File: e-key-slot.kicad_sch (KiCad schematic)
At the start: 27 parts, among them J1 MDT420E03002, J3 PJ-018, Q1 TSM9409CS, Q2 TSM9409CS, Q3 TSM9409CS, U1 TPS54331DRG4

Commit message: Add bounding boxes
Signed-off-by: JeffMboya <jangina.mboya@gmail.com>
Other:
- note added: "9v DC input"
- note added: "9v DC to 3v3 buck converter"
- note removed: "PCIe M.2 Key E Card Socket"
- moved on the sheet: J1

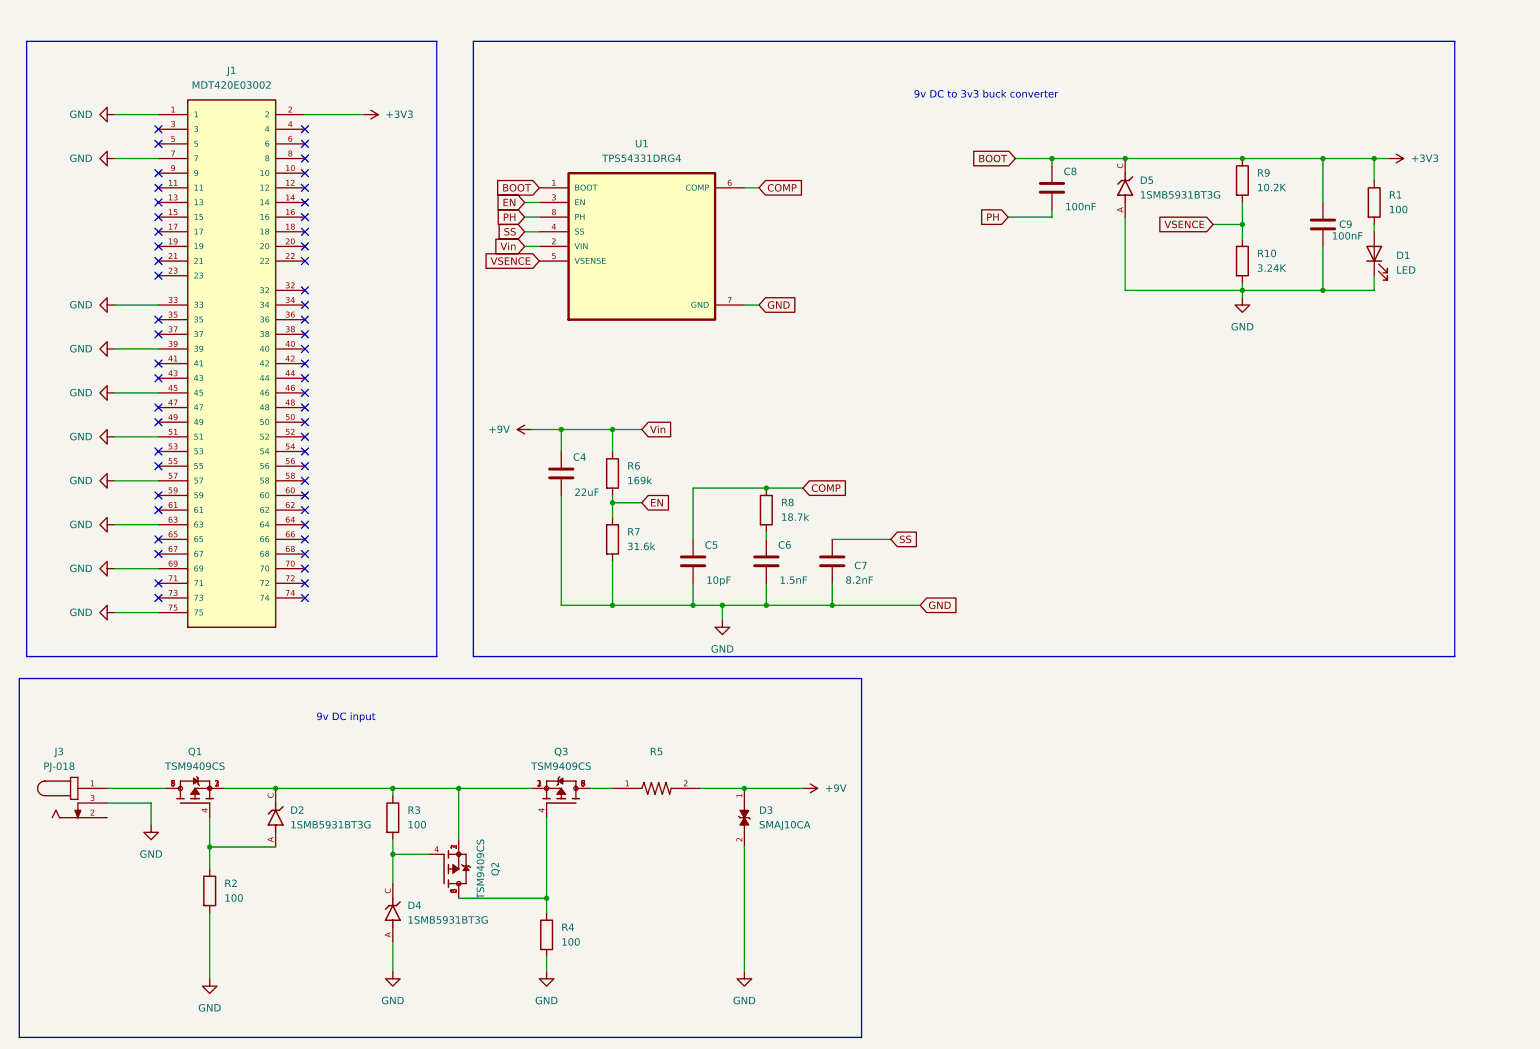
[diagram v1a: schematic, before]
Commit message: Add MCP73831
Signed-off-by: JeffMboya <jangina.mboya@gmail.com>
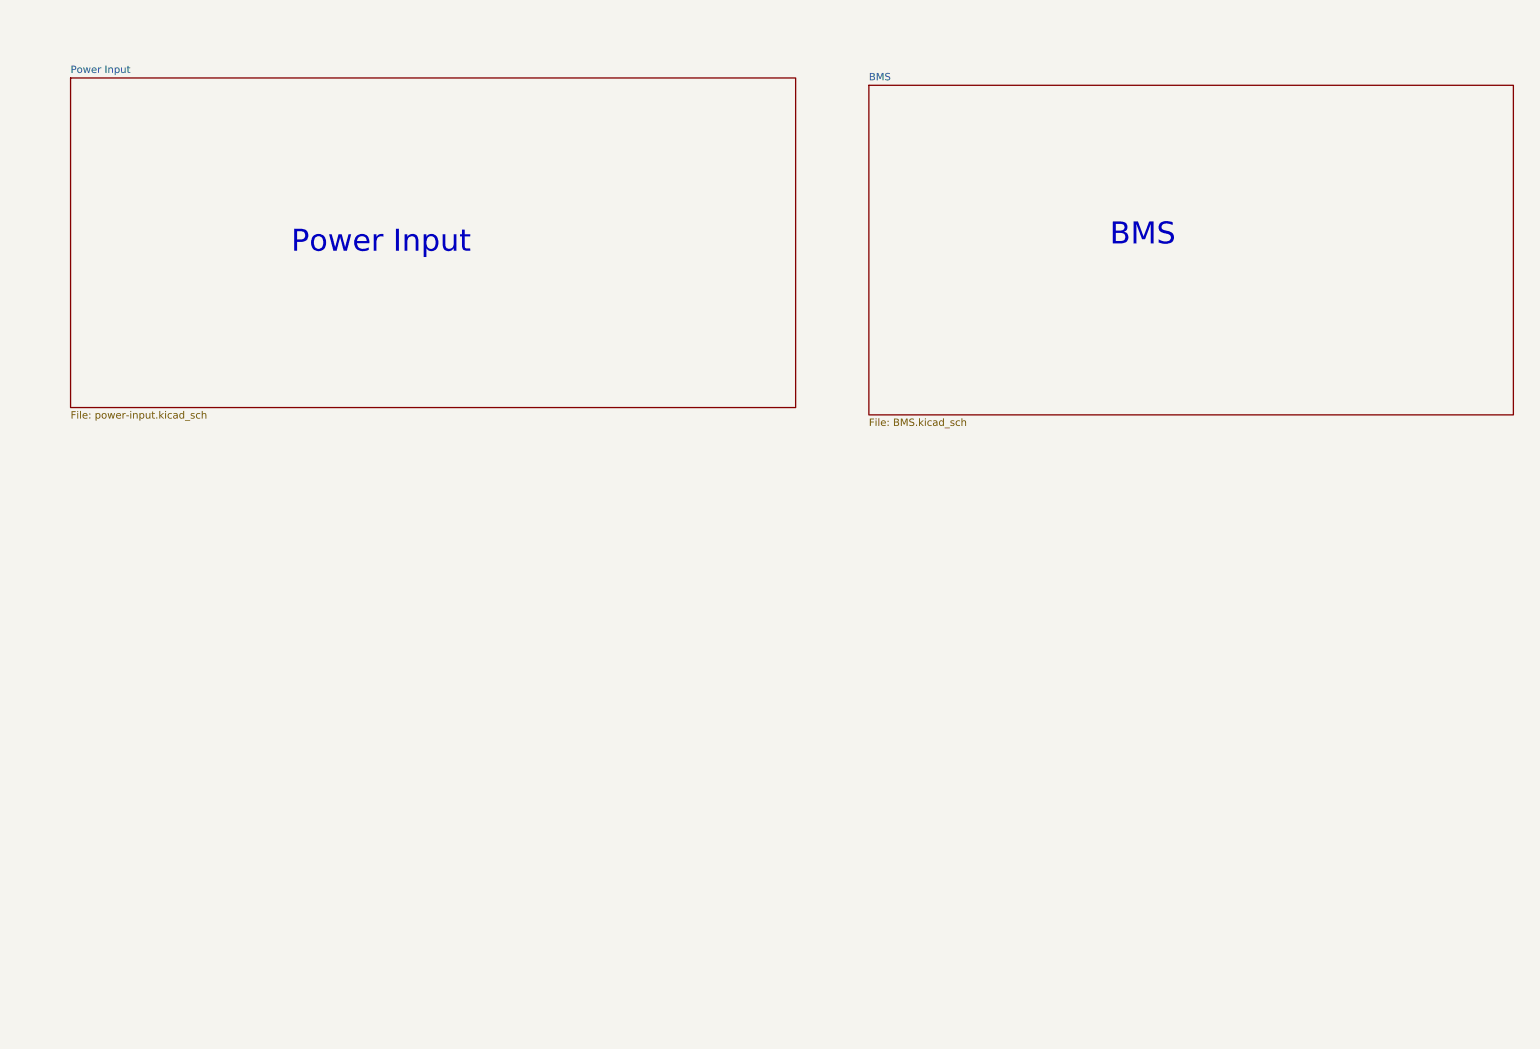
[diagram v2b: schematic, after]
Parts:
- removed C4: 22uF, Capacitor_SMD:C_1206_3216Metric, symbol Device:C
- removed C5: 10pF, Capacitor_SMD:C_1206_3216Metric, symbol Device:C
- removed C6: 1.5nF, Capacitor_SMD:C_1206_3216Metric, symbol Device:C
- removed C7: 8.2nF, Capacitor_SMD:C_1206_3216Metric, symbol Device:C
- removed C8, C9: 100nF, Capacitor_SMD:C_1206_3216Metric, symbol Device:C
- removed D1: LED, LED_SMD:LED_0603_1608Metric, symbol Device:LED
- removed D2, D4, D5: 1SMB5931BT3G, 1SMB5931BT3G:DIOM5436X247N, symbol 1SMB5931BT3G:1SMB5931BT3G
- removed D3: SMAJ10CA, SMAJ10CA:DIOM4325X250N, symbol SMAJ10CA:SMAJ10CA
- removed J1: MDT420E03002, MDT420E03002:AMPHENOL_MDT420E03002, symbol MDT420E03002:MDT420E03002
- removed J3: PJ-018, PJ-018:CUI_PJ-018, symbol PJ-018:PJ-018
- removed Q1, Q2, Q3: TSM9409CS, TSM9409CS:TRANS_TSM9409CS, symbol TSM9409CS:TSM9409CS
- removed R1, R2, R3, R4: 100, Resistor_SMD:R_0603_1608Metric, symbol Device:R
- removed R10: 3.24K, Resistor_SMD:R_0603_1608Metric, symbol Device:R
- removed R5: 0ZCA0100FF2E, 0ZCA0100FF2E:RESC3216X125N, symbol 0ZCA0100FF2E:0ZCA0100FF2E
- removed R6: 169k, Resistor_SMD:R_0603_1608Metric, symbol Device:R
- removed R7: 31.6k, Resistor_SMD:R_0603_1608Metric, symbol Device:R
- removed R8: 18.7k, Resistor_SMD:R_0603_1608Metric, symbol Device:R
- removed R9: 10.2K, Resistor_SMD:R_0603_1608Metric, symbol Device:R
- removed U1: TPS54331DRG4, TPS54331DRG4:SOIC127P599X175-8N, symbol TPS54331DRG4:TPS54331DRG4
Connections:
- no-connect marks 56 -> 0
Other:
- added sheet BMS (BMS.kicad_sch)
- added sheet Power Input (power-input.kicad_sch)
- note added: "BMS"
- note added: "Power Input"
- note removed: "9v DC input"
- note removed: "9v DC to 3v3 buck converter"

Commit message: Add BMS
Signed-off-by: JeffMboya <jangina.mboya@gmail.com>
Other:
- added sheet e-key-socket (e-key-socket.kicad_sch)
- note added: "E-key Socket"
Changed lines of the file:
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@@
 		(comment 2 "Approved By:")
+	)
+	(text "E-key Socket"
+		(exclude_from_sim no)
+		(at 87.122 114.046 0)
+		(effects
+			(font
+				(size 3.81 3.81)
+			)
+		)
 	)
 	(text "BMS\n"
@@
 				(size 3.81 3.81)
 				(color 0 0 0 1)
+			)
+		)
+	)
+	(sheet
+		(at 29.21 90.17)
+		(size 123.19 46.99)
+		(fields_autoplaced yes)
+		(stroke
+			(width 0.1524)
+			(type solid)
+		)
+		(fill
+			(color 110 39 255 1.0000)
+		)
+		(property "Sheetname" "e-key-socket"
+			(at 29.21 89.4584 0)
+			(effects
+				(font
+					(size 1.27 1.27)
+				)
+				(justify left bottom)
+			)
+		)
+		(property "Sheetfile" "e-key-socket.kicad_sch"
+			(at 29.21 137.7446 0)
+			(effects
+				(font
+					(size 1.27 1.27)
+				)
+				(justify left top)
+			)
+		)
+		(instances
+			(project "e-key-slot"
+				(path "/c124244a-3c1c-475d-932f-950445d8391e"
+					(page "4")
+				)
 			)
 		)
@@
 		)
 		(fill
-			(color 150 0 87 1.0000)
+			(color 150 55 37 1.0000)
 		)
 		(property "Sheetname" "Power Input"

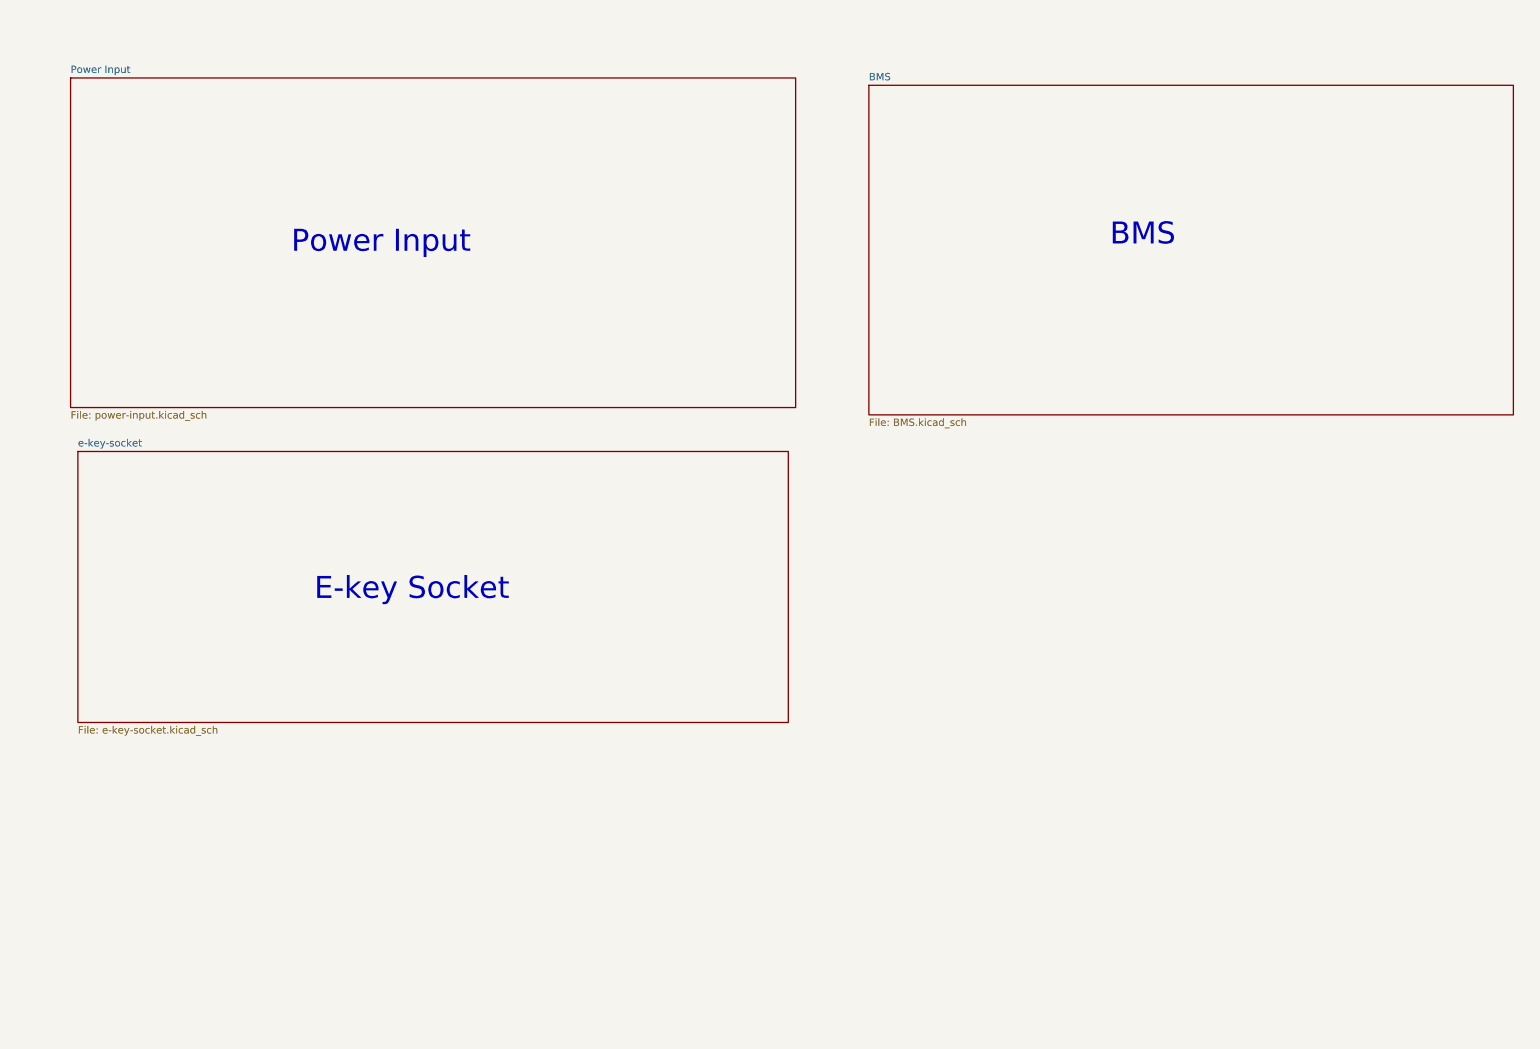
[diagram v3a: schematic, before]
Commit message: Delete BMS and Power input schematics
Signed-off-by: JeffMboya <jangina.mboya@gmail.com>
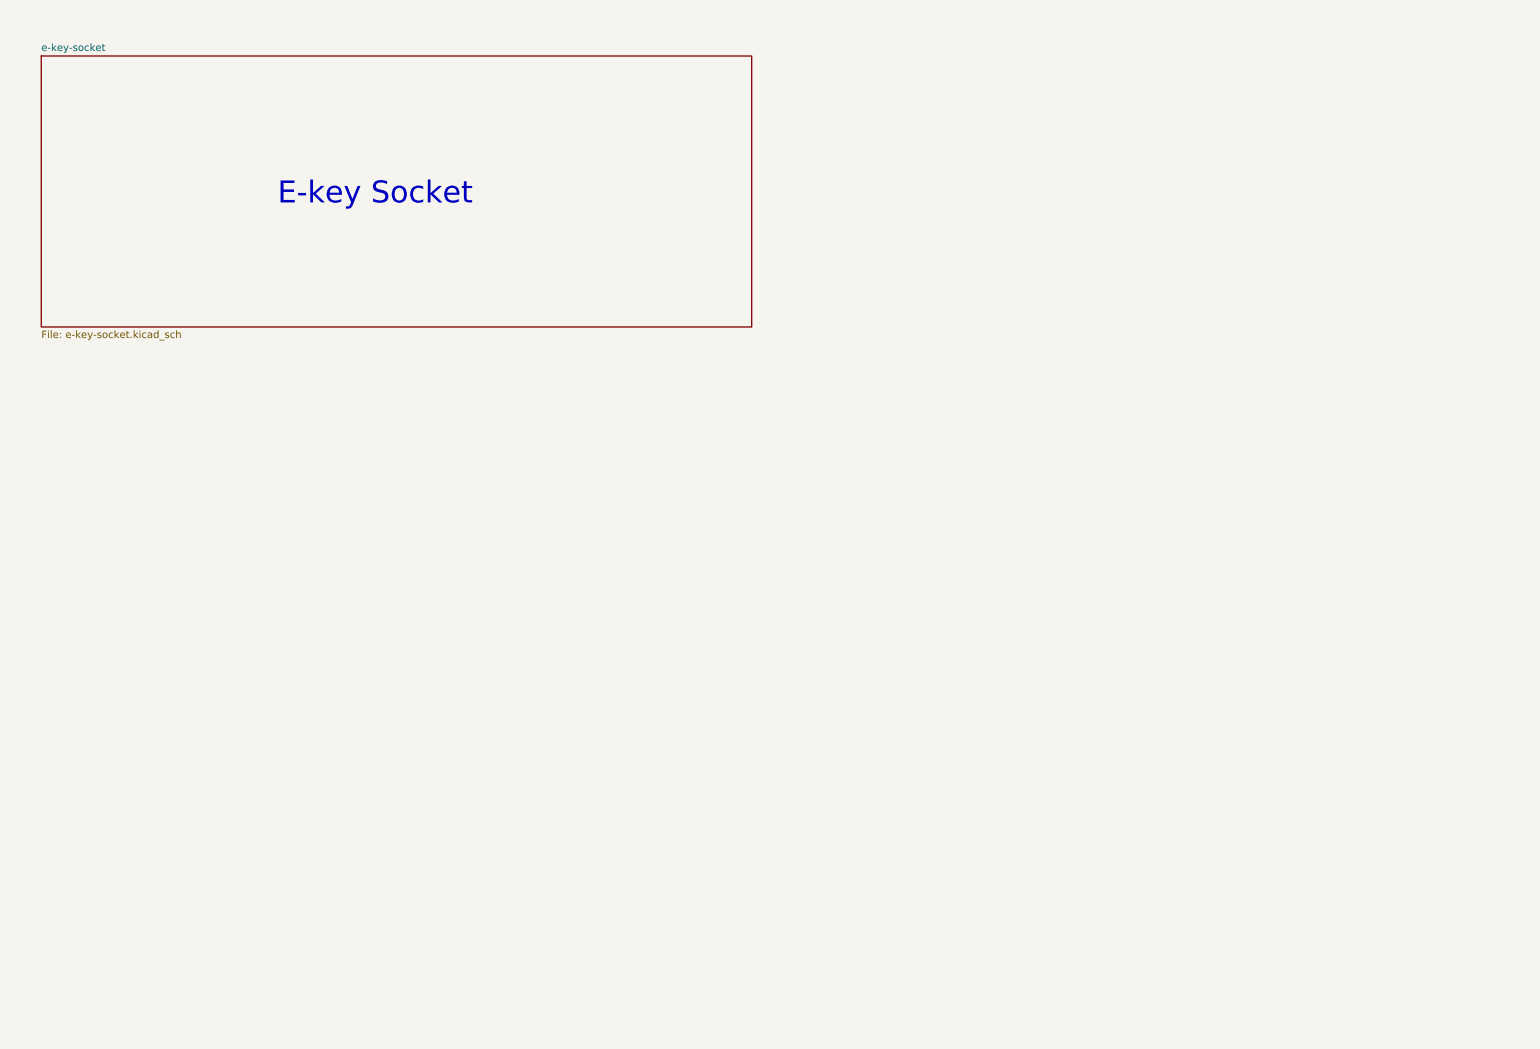
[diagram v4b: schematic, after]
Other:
- removed sheet BMS
- removed sheet Power Input
- note removed: "BMS"
- note removed: "Power Input"
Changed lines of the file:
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@@
 	(text "E-key Socket"
 		(exclude_from_sim no)
-		(at 87.122 114.046 0)
+		(at 80.772 45.466 0)
 		(effects
 			(font
@@
 		)
 	)
-	(text "BMS\n"
-		(exclude_from_sim no)
-		(at 213.868 52.578 0)
-		(effects
-			(font
-				(size 3.81 3.81)
-			)
-		)
-	)
-	(text "Power Input"
-		(exclude_from_sim no)
-		(at 81.788 53.848 0)
-		(effects
-			(font
-				(size 3.81 3.81)
-				(color 0 0 0 1)
-			)
-		)
-	)
 	(sheet
-		(at 29.21 90.17)
+		(at 22.86 21.59)
 		(size 123.19 46.99)
 		(fields_autoplaced yes)
@@
 		)
 		(fill
-			(color 110 39 255 1.0000)
+			(color 107 83 255 1.0000)
 		)
 		(property "Sheetname" "e-key-socket"
-			(at 29.21 89.4584 0)
+			(at 22.86 20.8784 0)
 			(effects
 				(font
@@
 		)
 		(property "Sheetfile" "e-key-socket.kicad_sch"
-			(at 29.21 137.7446 0)
+			(at 22.86 69.1646 0)
 			(effects
 				(font
@@
 				)
 			)
-		)
-	)
-	(sheet
-		(at 166.37 26.67)
-		(size 111.76 57.15)
-		(fields_autoplaced yes)
-		(stroke
-			(width 0.1524)
-			(type solid)
-		)
-		(fill
-			(color 0 150 0 1.0000)
-		)
-		(property "Sheetname" "BMS"
-			(at 166.37 25.9584 0)
-			(effects
-				(font
-					(size 1.27 1.27)
-				)
-				(justify left bottom)
-			)
-		)
-		(property "Sheetfile" "BMS.kicad_sch"
-			(at 166.37 84.4046 0)
-			(effects
-				(font
-					(size 1.27 1.27)
-				)
-				(justify left top)
-			)
-		)
-		(instances
-			(project "e-key-slot"
-				(path "/c124244a-3c1c-475d-932f-950445d8391e"
-					(page "3")
-				)
-			)
-		)
-	)
-	(sheet
-		(at 27.94 25.4)
-		(size 125.73 57.15)
-		(fields_autoplaced yes)
-		(stroke
-			(width 0.1524)
-			(type solid)
-		)
-		(fill
-			(color 150 55 37 1.0000)
-		)
-		(property "Sheetname" "Power Input"
-			(at 27.94 24.6884 0)
-			(effects
-				(font
-					(size 1.27 1.27)
-				)
-				(justify left bottom)
-			)
-		)
-		(property "Sheetfile" "power-input.kicad_sch"
-			(at 27.94 83.1346 0)
-			(effects
-				(font
-					(size 1.27 1.27)
-				)
-				(justify left top)
-			)
-		)
-		(property "Field2" ""
-			(at 27.94 25.4 0)
-			(effects
-				(font
-					(size 1.27 1.27)
-				)
-				(hide yes)
-			)
-		)
-		(instances
-			(project "e-key-slot"
-				(path "/c124244a-3c1c-475d-932f-950445d8391e"
-					(page "2")
-				)
-			)

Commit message: Add 1048P
Signed-off-by: JeffMboya <jangina.mboya@gmail.com>
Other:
- added sheet Power Input (power-input.kicad_sch)
- note added: "Power Input"
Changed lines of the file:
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@@
 	(text "E-key Socket"
 		(exclude_from_sim no)
-		(at 80.772 45.466 0)
+		(at 215.392 49.276 0)
 		(effects
 			(font
@@
 		)
 	)
+	(text "Power Input"
+		(exclude_from_sim no)
+		(at 71.628 52.578 0)
+		(effects
+			(font
+				(size 3.81 3.81)
+				(color 0 0 0 1)
+			)
+		)
+	)
 	(sheet
-		(at 22.86 21.59)
-		(size 123.19 46.99)
+		(at 158.75 25.4)
+		(size 121.92 55.88)
 		(fields_autoplaced yes)
 		(stroke
@@
 		)
 		(fill
-			(color 107 83 255 1.0000)
+			(color 110 39 255 1.0000)
 		)
 		(property "Sheetname" "e-key-socket"
-			(at 22.86 20.8784 0)
+			(at 158.75 24.6884 0)
 			(effects
 				(font
@@
 		)
 		(property "Sheetfile" "e-key-socket.kicad_sch"
-			(at 22.86 69.1646 0)
+			(at 158.75 81.8646 0)
 			(effects
 				(font
@@
 				)
 			)
+		)
+	)
+	(sheet
+		(at 17.78 24.13)
+		(size 125.73 57.15)
+		(fields_autoplaced yes)
+		(stroke
+			(width 0.1524)
+			(type solid)
+		)
+		(fill
+			(color 150 55 37 1.0000)
+		)
+		(property "Sheetname" "Power Input"
+			(at 17.78 23.4184 0)
+			(effects
+				(font
+					(size 1.27 1.27)
+				)
+				(justify left bottom)
+			)
+		)
+		(property "Sheetfile" "power-input.kicad_sch"
+			(at 17.78 81.8646 0)
+			(effects
+				(font
+					(size 1.27 1.27)
+				)
+				(justify left top)
+			)
+		)
+		(property "Field2" ""
+			(at 17.78 24.13 0)
+			(effects
+				(font
+					(size 1.27 1.27)
+				)
+				(hide yes)
+			)
+		)
+		(instances
+			(project "e-key-slot"
+				(path "/c124244a-3c1c-475d-932f-950445d8391e"
+					(page "2")
+				)
+			)
